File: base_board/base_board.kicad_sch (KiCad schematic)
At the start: 61 parts, among them J1 Conn_ARM_JTAG_SWD_20, J3 Conn_01x04, SW1 SW_Push, U1 STM32F446ZEJx, U2 IS42S16400J-xT, U3 BMI270, U4 USB_C_Receptacle_USB2.0, U5 10p, U6 10p, U7 LD3985M33R_SOT23, Y1 Crystal_GND24

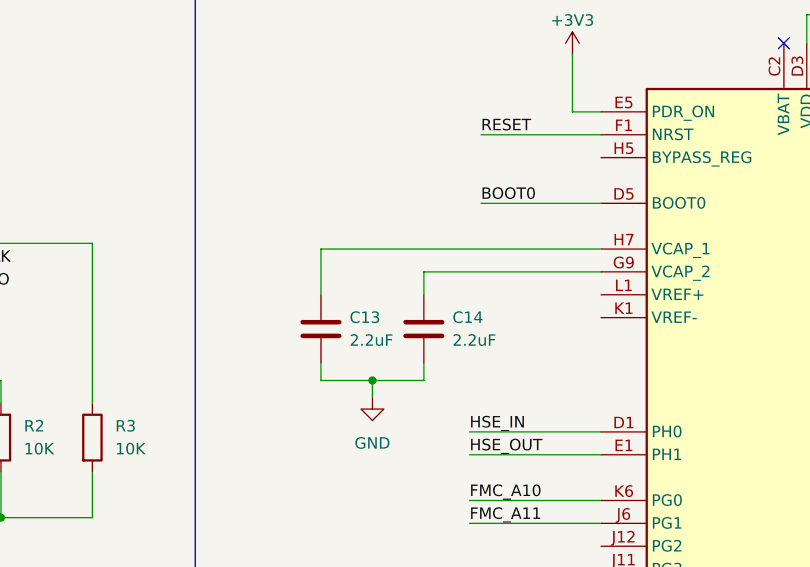
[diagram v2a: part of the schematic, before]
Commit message: [pcb][schematic] fixed VREF connection. Corrected the shape of the length matcher
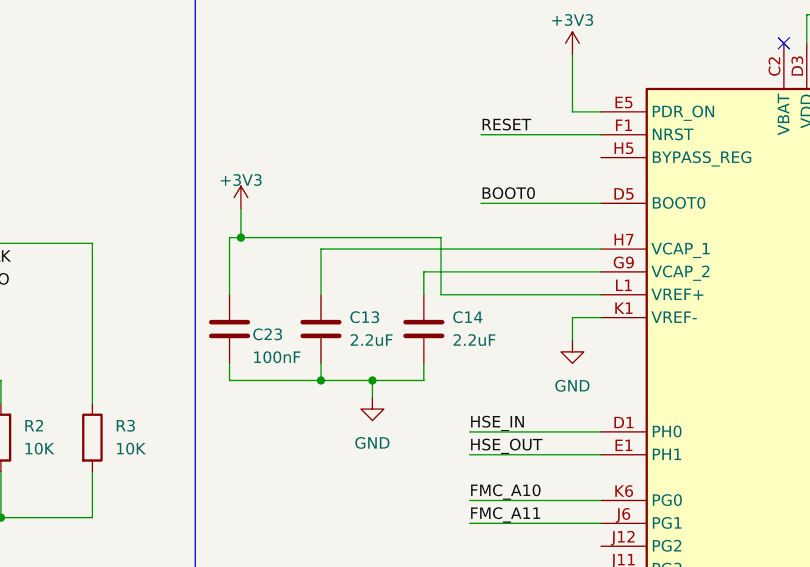
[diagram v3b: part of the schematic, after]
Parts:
- added C23: 100nF, Capacitor_SMD:C_0603_1608Metric, symbol Device:C
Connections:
- net +3V3: now also U1.L1 (VREF+), C23.1
- net GND: now also U1.K1 (VREF-), C23.2
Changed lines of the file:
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@@
   (junction (at 243.205 20.955) (diameter 0) (color 0 0 0 0)
   )
+  (junction (at 98.425 44.45) (diameter 0) (color 0 0 0 0)
+  )
   (junction (at 166.37 19.685) (diameter 0) (color 0 0 0 0)
   )
@@
   (junction (at 34.29 125.095) (diameter 0) (color 0 0 0 0)
   )
+  (junction (at 107.315 60.325) (diameter 0) (color 0 0 0 0)
+  )
   (junction (at 297.18 165.1) (diameter 0) (color 0 0 0 0)
   )
@@
     (stroke (width 0) (type default))
   )
+  (wire (pts (xy 98.425 44.45) (xy 97.155 44.45))
+    (stroke (width 0) (type default))
+  )
   (wire (pts (xy 123.825 68.58) (xy 138.43 68.58))
     (stroke (width 0) (type default))
@@
     (stroke (width 0) (type default))
   )
+  (wire (pts (xy 98.425 41.275) (xy 98.425 44.45))
+    (stroke (width 0) (type default))
+  )
   (wire (pts (xy 64.77 171.45) (xy 64.77 173.99))
     (stroke (width 0) (type default))
@@
     (stroke (width 0) (type default))
   )
+  (wire (pts (xy 135.255 53.34) (xy 135.255 55.88))
+    (stroke (width 0) (type default))
+  )
   (wire (pts (xy 89.535 128.27) (xy 92.075 128.27))
     (stroke (width 0) (type default))
@@
     (stroke (width 0) (type default))
   )
+  (wire (pts (xy 97.155 60.325) (xy 107.315 60.325))
+    (stroke (width 0) (type default))
+  )
   (wire (pts (xy 204.47 111.76) (xy 222.25 111.76))
     (stroke (width 0) (type default))
@@
     (stroke (width 0) (type default))
   )
+  (wire (pts (xy 120.65 44.45) (xy 98.425 44.45))
+    (stroke (width 0) (type default))
+  )
   (wire (pts (xy 204.47 83.82) (xy 222.25 83.82))
     (stroke (width 0) (type default))
@@
     (stroke (width 0) (type default))
   )
+  (wire (pts (xy 138.43 50.8) (xy 120.65 50.8))
+    (stroke (width 0) (type default))
+  )
   (wire (pts (xy 166.37 260.985) (xy 173.99 260.985))
     (stroke (width 0) (type default))
@@
     (stroke (width 0) (type default))
   )
+  (wire (pts (xy 97.155 58.42) (xy 97.155 60.325))
+    (stroke (width 0) (type default))
+  )
   (wire (pts (xy 204.47 132.08) (xy 212.09 132.08))
     (stroke (width 0) (type default))
@@
     (stroke (width 0) (type default))
   )
+  (wire (pts (xy 138.43 53.34) (xy 135.255 53.34))
+    (stroke (width 0) (type default))
+  )
   (wire (pts (xy 171.45 205.74) (xy 171.45 209.55))
     (stroke (width 0) (type default))
@@
     (stroke (width 0) (type default))
   )
+  (wire (pts (xy 97.155 44.45) (xy 97.155 50.8))
+    (stroke (width 0) (type default))
+  )
   (wire (pts (xy 123.825 198.12) (xy 138.43 198.12))
     (stroke (width 0) (type default))
@@
     (stroke (width 0) (type default))
   )
+  (wire (pts (xy 120.65 50.8) (xy 120.65 44.45))
+    (stroke (width 0) (type default))
+  )
   (wire (pts (xy 257.81 77.47) (xy 275.59 77.47))
     (stroke (width 0) (type default))
@@
     )
   )
+  (symbol (lib_name "GND_3") (lib_id "power:GND") (at 135.255 55.88 0) (unit 1)
+    (in_bom yes) (on_board yes) (dnp no) (fields_autoplaced)
+    (property "Reference" "#PWR012" (at 135.255 62.23 0)
+      (effects (font (size 1.27 1.27)) hide)
+    )
+    (property "Value" "GND" (at 135.255 60.96 0)
+      (effects (font (size 1.27 1.27)))
+    )
+    (property "Footprint" "" (at 135.255 55.88 0)
+      (effects (font (size 1.27 1.27)) hide)
+    )
+    (property "Datasheet" "" (at 135.255 55.88 0)
+      (effects (font (size 1.27 1.27)) hide)
+    )
+    (pin "1")
+    (instances
+      (project "base_board"
+        (path "/2307506f-1d7e-4fdb-b101-b9905788fe29"
+          (reference "#PWR012") (unit 1)
+        )
+      )
+    )
+  )
   (symbol (lib_id "Device:C") (at 271.78 154.94 0) (unit 1)
     (in_bom yes) (on_board yes) (dnp no) (fields_autoplaced)
@@
     )
   )
+  (symbol (lib_id "Device:C") (at 97.155 54.61 0) (unit 1)
+    (in_bom yes) (on_board yes) (dnp no)
+    (property "Reference" "C23" (at 99.695 55.245 0)
+      (effects (font (size 1.27 1.27)) (justify left))
+    )
+    (property "Value" "100nF" (at 99.695 57.785 0)
+      (effects (font (size 1.27 1.27)) (justify left))
+    )
+    (property "Footprint" "Capacitor_SMD:C_0603_1608Metric" (at 98.1202 58.42 0)
+      (effects (font (size 1.27 1.27)) hide)
+    )
+    (property "Datasheet" "~" (at 97.155 54.61 0)
+      (effects (font (size 1.27 1.27)) hide)
+    )
+    (pin "1")
+    (pin "2")
+    (instances
+      (project "base_board"
+        (path "/2307506f-1d7e-4fdb-b101-b9905788fe29"
+          (reference "C23") (unit 1)
+        )
+      )
+    )
+  )
   (symbol (lib_id "Device:LED") (at 267.97 257.81 180) (unit 1)
     (in_bom yes) (on_board yes) (dnp no) (fields_autoplaced)
@@
         )
       )
+    )
+  )
+  (symbol (lib_name "+3V3_9") (lib_id "power:+3V3") (at 98.425 41.275 0) (unit 1)
+    (in_bom yes) (on_board yes) (dnp no) (fields_autoplaced)
+    (property "Reference" "#PWR013" (at 98.425 45.085 0)
+      (effects (font (size 1.27 1.27)) hide)
+    )
+    (property "Value" "+3V3" (at 98.425 38.1 0)
+      (effects (font (size 1.27 1.27)))
+    )
+    (property "Footprint" "" (at 98.425 41.275 0)
+      (effects (font (size 1.27 1.27)) hide)
+    )
+    (property "Datasheet" "" (at 98.425 41.275 0)
+      (effects (font (size 1.27 1.27)) hide)
+    )
+    (pin "1")
+    (instances
+      (project "base_board"
+        (path "/2307506f-1d7e-4fdb-b101-b9905788fe29"
+          (reference "#PWR013") (unit 1)
+        )
+      )
